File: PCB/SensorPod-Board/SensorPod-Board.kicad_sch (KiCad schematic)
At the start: 12 parts, among them J1 Board Header, J2 EXT I2C, J3 Reset, J4 Backup DC, U1 Pico W, U2 SCD30, U3 LM1117-3.3

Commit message: Board fixes
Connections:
- net at J2.2 (Pin_2), R2.2: now also U1.5 (GPIO3); no longer U1.9 (GPIO6), U2.4 (RX/SDA)
- net at J2.3 (Pin_3), R1.2: now also U1.4 (GPIO2); no longer U1.5 (GPIO3), U2.3 (TX/SCL)
- net at U1.6 (GPIO4): now also U2.4 (RX/SDA)
- net at U1.7 (GPIO5): now also U2.3 (TX/SCL)
- no-connect marks 29 -> 27
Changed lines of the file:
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@@
   (junction (at 204.47 39.37) (diameter 0) (color 0 0 0 0)
   )
+  (junction (at 121.92 69.85) (diameter 0) (color 0 0 0 0)
+  )
   (junction (at 90.17 142.24) (diameter 0) (color 0 0 0 0)
   )
@@
   (junction (at 193.04 85.09) (diameter 0) (color 0 0 0 0)
   )
-  (junction (at 129.54 67.31) (diameter 0) (color 0 0 0 0)
-  )
-  (junction (at 132.08 90.17) (diameter 0) (color 0 0 0 0)
+  (junction (at 127 67.31) (diameter 0) (color 0 0 0 0)
   )
   (junction (at 143.51 39.37) (diameter 0) (color 0 0 0 0)
   )
-  (junction (at 134.62 100.33) (diameter 0) (color 0 0 0 0)
-  )
-  (junction (at 121.92 69.85) (diameter 0) (color 0 0 0 0)
-  )
   (junction (at 140.97 97.79) (diameter 0) (color 0 0 0 0)
   )
@@
   )
   (no_connect (at 182.88 87.63))
-  (no_connect (at 147.32 95.25))
   (no_connect (at 147.32 102.87))
   (no_connect (at 147.32 105.41))
@@
   (no_connect (at 147.32 128.27))
   (no_connect (at 147.32 125.73))
-  (no_connect (at 147.32 92.71))
   (no_connect (at 182.88 102.87))
   (no_connect (at 182.88 105.41))
@@
   (no_connect (at 182.88 90.17))
   (no_connect (at 182.88 80.01))
+  (no_connect (at 147.32 100.33))
   (no_connect (at 95.25 102.87))
   (no_connect (at 95.25 97.79))
-  (no_connect (at 147.32 87.63))
   (wire (pts (xy 181.61 39.37) (xy 181.61 55.88))
     (stroke (width 0) (type default) (color 0 0 0 0))
@@
     (stroke (width 0) (type default) (color 0 0 0 0))
   )
+  (wire (pts (xy 137.16 102.87) (xy 137.16 95.25))
+    (stroke (width 0) (type default) (color 0 0 0 0))
+  )
   (wire (pts (xy 73.66 54.61) (xy 73.66 50.8))
     (stroke (width 0) (type default) (color 0 0 0 0))
@@
     (stroke (width 0) (type default) (color 0 0 0 0))
   )
+  (wire (pts (xy 129.54 87.63) (xy 129.54 69.85))
+    (stroke (width 0) (type default) (color 0 0 0 0))
+  )
   (wire (pts (xy 181.61 55.88) (xy 186.69 55.88))
     (stroke (width 0) (type default) (color 0 0 0 0))
@@
     (stroke (width 0) (type default) (color 0 0 0 0))
   )
+  (wire (pts (xy 134.62 105.41) (xy 134.62 92.71))
+    (stroke (width 0) (type default) (color 0 0 0 0))
+  )
   (wire (pts (xy 181.61 39.37) (xy 204.47 39.37))
     (stroke (width 0) (type default) (color 0 0 0 0))
   )
+  (wire (pts (xy 134.62 92.71) (xy 147.32 92.71))
+    (stroke (width 0) (type default) (color 0 0 0 0))
+  )
   (wire (pts (xy 162.56 133.35) (xy 162.56 137.16))
     (stroke (width 0) (type default) (color 0 0 0 0))
@@
     (stroke (width 0) (type default) (color 0 0 0 0))
   )
-  (wire (pts (xy 129.54 67.31) (xy 129.54 87.63))
-    (stroke (width 0) (type default) (color 0 0 0 0))
-  )
   (wire (pts (xy 182.88 85.09) (xy 193.04 85.09))
     (stroke (width 0) (type default) (color 0 0 0 0))
@@
     (stroke (width 0) (type default) (color 0 0 0 0))
   )
-  (wire (pts (xy 134.62 100.33) (xy 147.32 100.33))
-    (stroke (width 0) (type default) (color 0 0 0 0))
-  )
   (wire (pts (xy 167.64 139.7) (xy 85.09 139.7))
     (stroke (width 0) (type default) (color 0 0 0 0))
@@
     (stroke (width 0) (type default) (color 0 0 0 0))
   )
-  (wire (pts (xy 134.62 87.63) (xy 134.62 100.33))
-    (stroke (width 0) (type default) (color 0 0 0 0))
-  )
   (wire (pts (xy 146.05 69.85) (xy 190.5 69.85))
     (stroke (width 0) (type default) (color 0 0 0 0))
   )
-  (wire (pts (xy 132.08 90.17) (xy 147.32 90.17))
-    (stroke (width 0) (type default) (color 0 0 0 0))
-  )
   (wire (pts (xy 146.05 58.42) (xy 146.05 69.85))
     (stroke (width 0) (type default) (color 0 0 0 0))
@@
     (stroke (width 0) (type default) (color 0 0 0 0))
   )
-  (wire (pts (xy 121.92 69.85) (xy 132.08 69.85))
+  (wire (pts (xy 127 90.17) (xy 147.32 90.17))
     (stroke (width 0) (type default) (color 0 0 0 0))
   )
@@
     (stroke (width 0) (type default) (color 0 0 0 0))
   )
+  (wire (pts (xy 121.92 69.85) (xy 129.54 69.85))
+    (stroke (width 0) (type default) (color 0 0 0 0))
+  )
   (wire (pts (xy 147.32 82.55) (xy 140.97 82.55))
     (stroke (width 0) (type default) (color 0 0 0 0))
@@
     (stroke (width 0) (type default) (color 0 0 0 0))
   )
-  (wire (pts (xy 132.08 69.85) (xy 132.08 90.17))
-    (stroke (width 0) (type default) (color 0 0 0 0))
-  )
   (wire (pts (xy 138.43 80.01) (xy 147.32 80.01))
     (stroke (width 0) (type default) (color 0 0 0 0))
@@
     (stroke (width 0) (type default) (color 0 0 0 0))
   )
-  (wire (pts (xy 120.65 67.31) (xy 129.54 67.31))
+  (wire (pts (xy 120.65 67.31) (xy 127 67.31))
     (stroke (width 0) (type default) (color 0 0 0 0))
   )
@@
     (stroke (width 0) (type default) (color 0 0 0 0))
   )
+  (wire (pts (xy 127 67.31) (xy 129.54 67.31))
+    (stroke (width 0) (type default) (color 0 0 0 0))
+  )
   (wire (pts (xy 140.97 110.49) (xy 147.32 110.49))
     (stroke (width 0) (type default) (color 0 0 0 0))
@@
     (stroke (width 0) (type default) (color 0 0 0 0))
   )
-  (wire (pts (xy 125.73 102.87) (xy 132.08 102.87))
-    (stroke (width 0) (type default) (color 0 0 0 0))
-  )
   (wire (pts (xy 140.97 57.15) (xy 140.97 82.55))
     (stroke (width 0) (type default) (color 0 0 0 0))
   )
-  (wire (pts (xy 132.08 102.87) (xy 132.08 90.17))
-    (stroke (width 0) (type default) (color 0 0 0 0))
-  )
   (wire (pts (xy 120.65 64.77) (xy 135.89 64.77))
     (stroke (width 0) (type default) (color 0 0 0 0))
@@
     (stroke (width 0) (type default) (color 0 0 0 0))
   )
-  (wire (pts (xy 134.62 100.33) (xy 134.62 105.41))
+  (wire (pts (xy 137.16 95.25) (xy 147.32 95.25))
     (stroke (width 0) (type default) (color 0 0 0 0))
   )
@@
     (stroke (width 0) (type default) (color 0 0 0 0))
   )
+  (wire (pts (xy 127 67.31) (xy 127 90.17))
+    (stroke (width 0) (type default) (color 0 0 0 0))
+  )
   (wire (pts (xy 158.75 39.37) (xy 181.61 39.37))
     (stroke (width 0) (type default) (color 0 0 0 0))
@@
     (stroke (width 0) (type default) (color 0 0 0 0))
   )
-  (wire (pts (xy 129.54 87.63) (xy 134.62 87.63))
-    (stroke (width 0) (type default) (color 0 0 0 0))
-  )
   (wire (pts (xy 90.17 92.71) (xy 95.25 92.71))
     (stroke (width 0) (type default) (color 0 0 0 0))
   )
+  (wire (pts (xy 125.73 102.87) (xy 137.16 102.87))
+    (stroke (width 0) (type default) (color 0 0 0 0))
+  )
   (wire (pts (xy 219.71 41.91) (xy 219.71 66.04))
     (stroke (width 0) (type default) (color 0 0 0 0))
   )
+  (wire (pts (xy 147.32 87.63) (xy 129.54 87.63))
+    (stroke (width 0) (type default) (color 0 0 0 0))
+  )

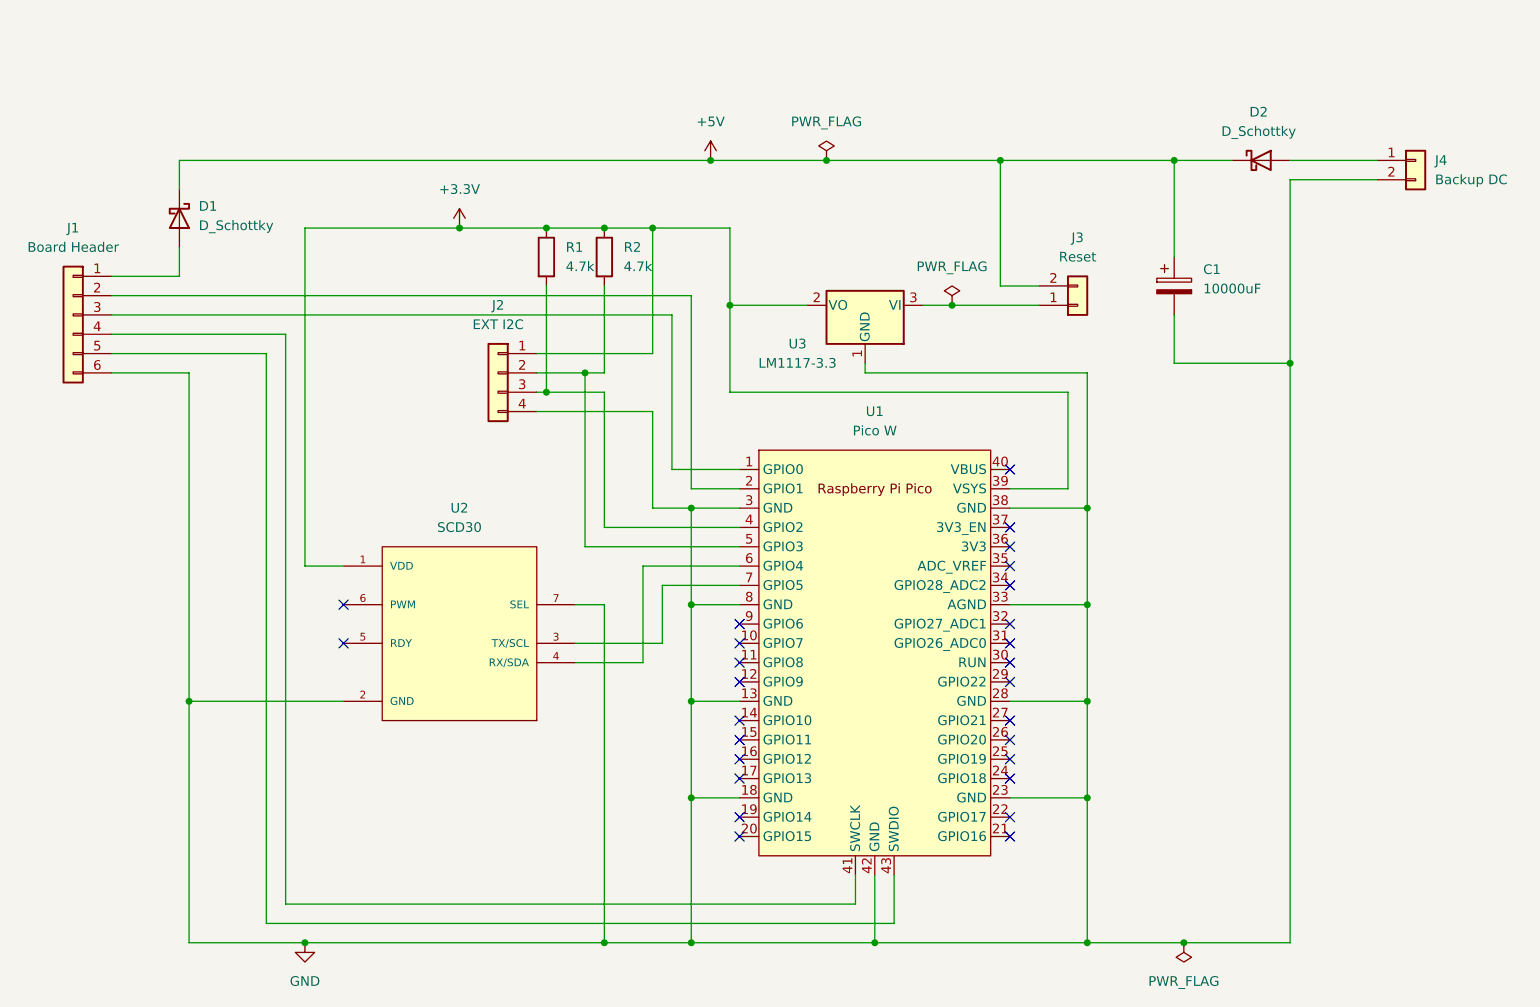
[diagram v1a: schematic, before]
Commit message: Better board version. Power cycling of sensor controlled by Pico.
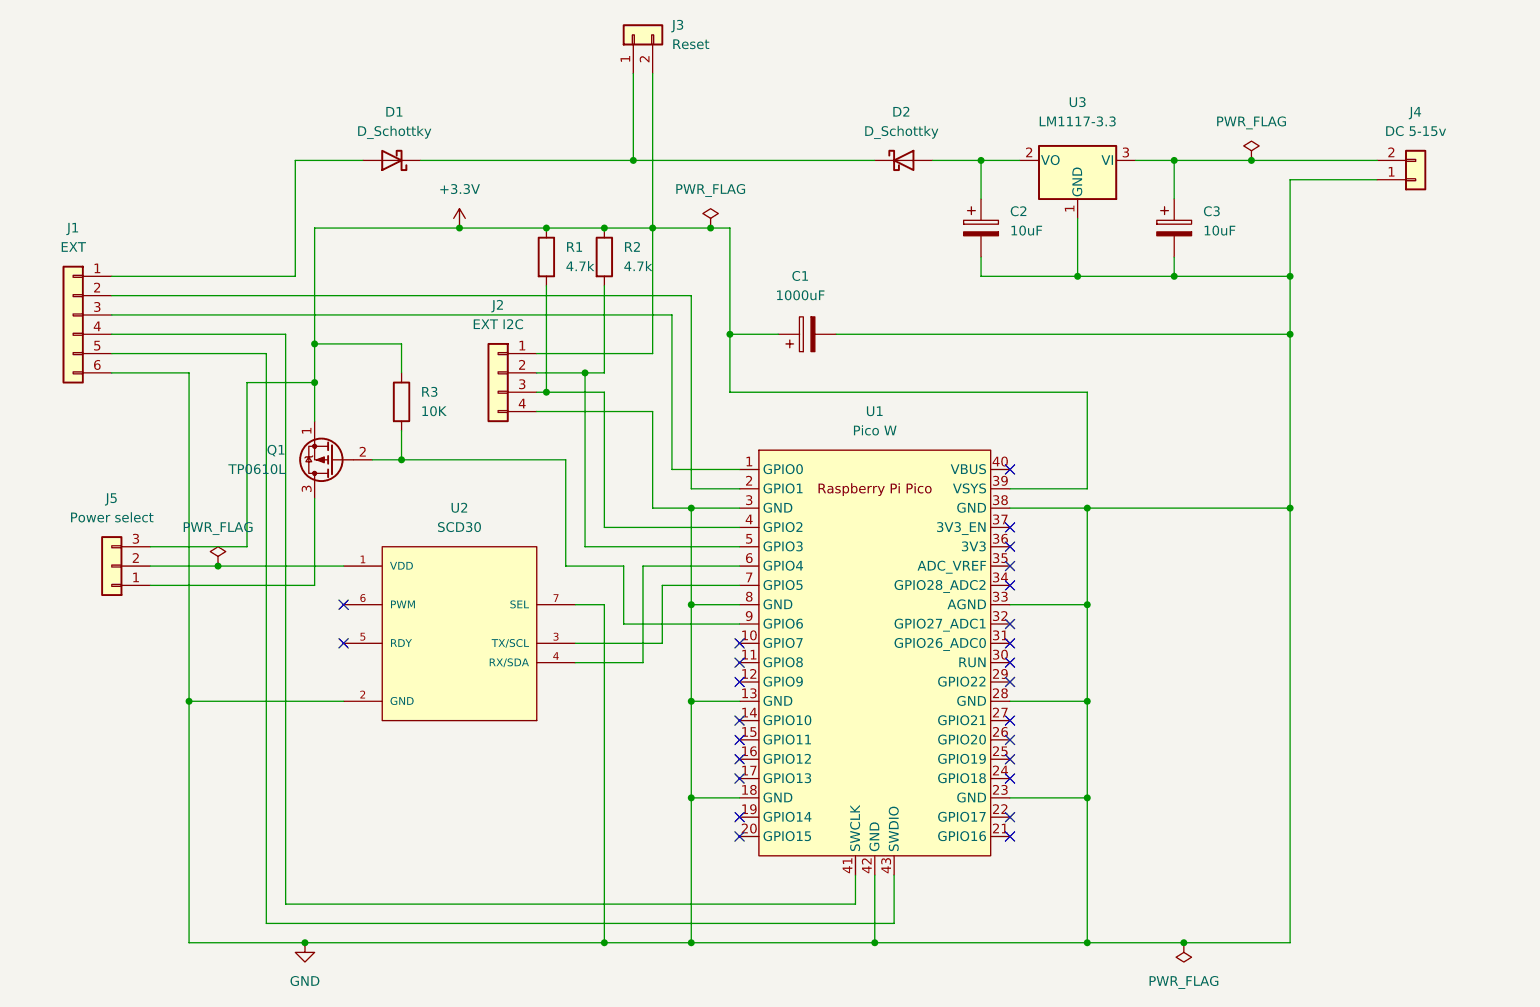
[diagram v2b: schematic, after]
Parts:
- added C2, C3: 10uF, Capacitor_THT:C_Radial_D6.3mm_H5.0mm_P2.50mm, symbol Device:C_Polarized
- added J5: Power select, Connector_PinHeader_2.54mm:PinHeader_1x03_P2.54mm_Vertical, symbol Connector_Generic:Conn_01x03
- added Q1: TP0610L, Package_TO_SOT_THT:TO-92L_Inline, symbol Transistor_FET:TP0610L
- added R3: 10K, Resistor_THT:R_Axial_DIN0207_L6.3mm_D2.5mm_P7.62mm_Horizontal, symbol Device:R
- C1: value 10000uF -> 1000uF
- J1: value Board Header -> EXT
- J4: value Backup DC -> DC 5-15v
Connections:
- net +3.3V: now also C1.1, J3.2 (Pin_2), J5.3 (Pin_3), Q1.1 (S), R3.1; no longer U2.1 (VDD), U3.2 (VO)
- net GND: now also J4.1 (Pin_1), C2.2, C3.2; no longer J4.2 (Pin_2)
- net at D2.2 (A): now also U3.2 (VO), C2.1; no longer J4.1 (Pin_1)
- net at J3.1 (Pin_1): now also D1.1 (K), D2.1 (K); no longer U3.3 (VI)
- net at U1.9 (GPIO6): now also Q1.2 (G), R3.2
- removed net +5V: C1.1, D1.1 (K), D2.1 (K), J3.2 (Pin_2)
- new net: J5.1 (Pin_1), Q1.3 (D)
- new net: C3.1, J4.2 (Pin_2), U3.3 (VI)
- new net: J5.2 (Pin_2), U2.1 (VDD)
- no-connect marks 27 -> 26
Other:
- moved on the sheet: D1, D2, J3, U3
